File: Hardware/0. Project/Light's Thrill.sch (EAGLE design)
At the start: 41 parts, among them CN1 Micro-USB, CN2 2.1MMJACKTHM, CN3 2x3, Q1 SI2302DS, Q2 SI2302DS, Q3 SI2302DS, U1 TSOP1838, U2 ATMEGA32U4, U3 LM1117-5.0, Y1 16 MHz

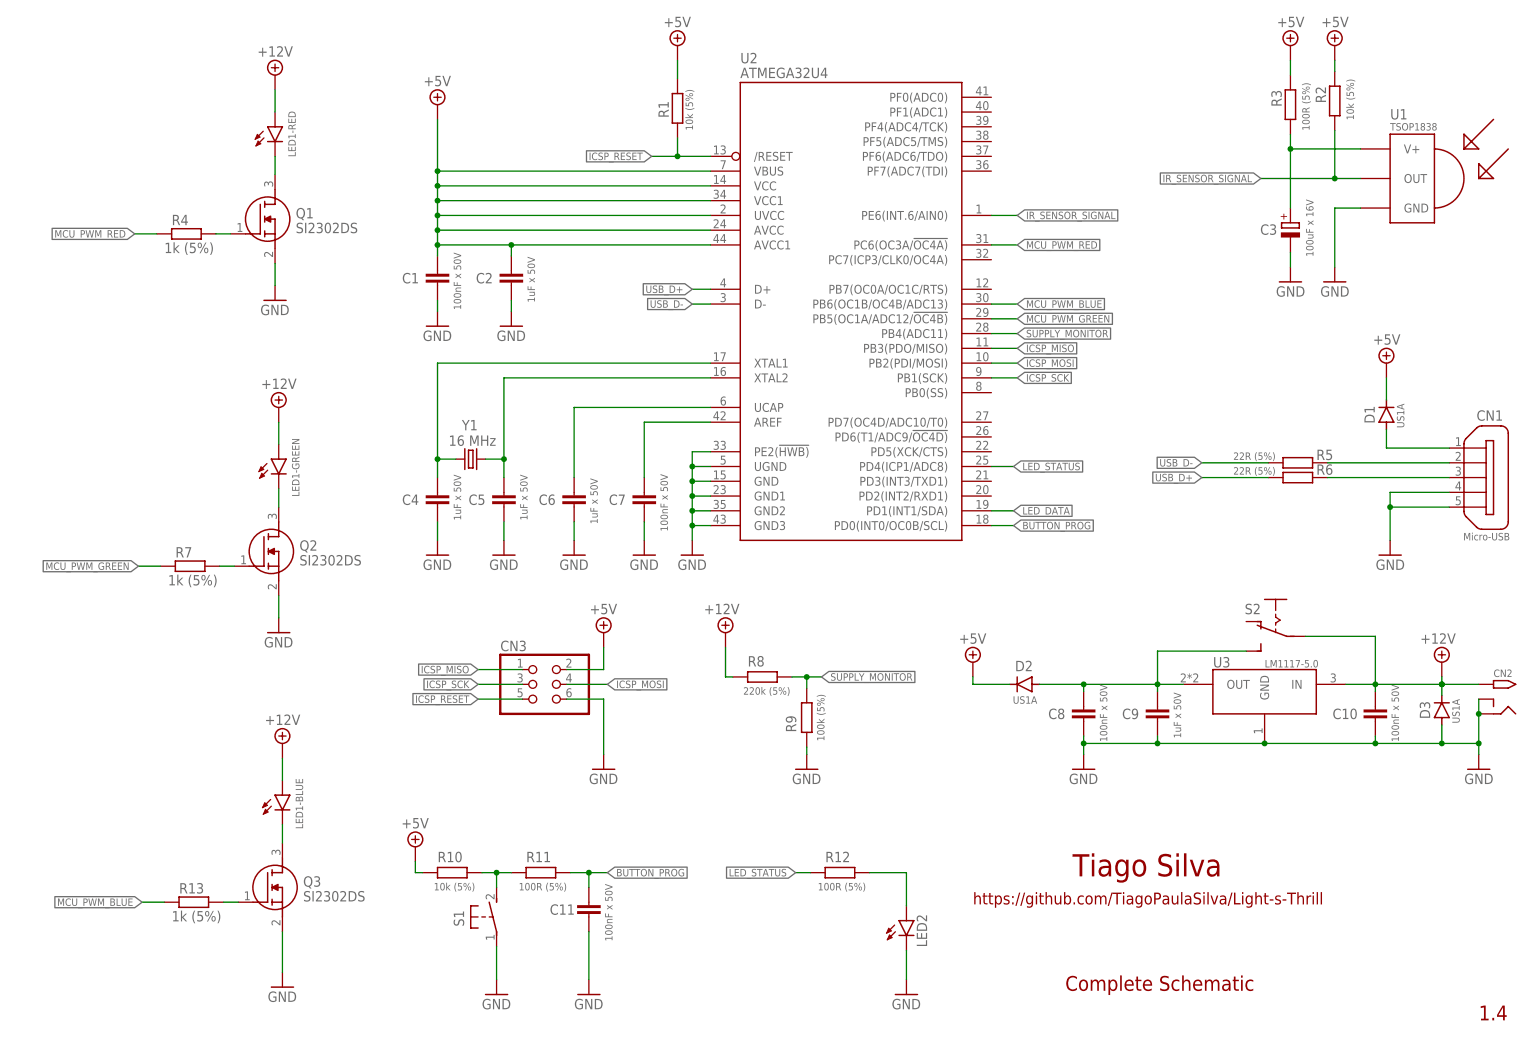
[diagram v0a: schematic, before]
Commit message: New images and directory structure
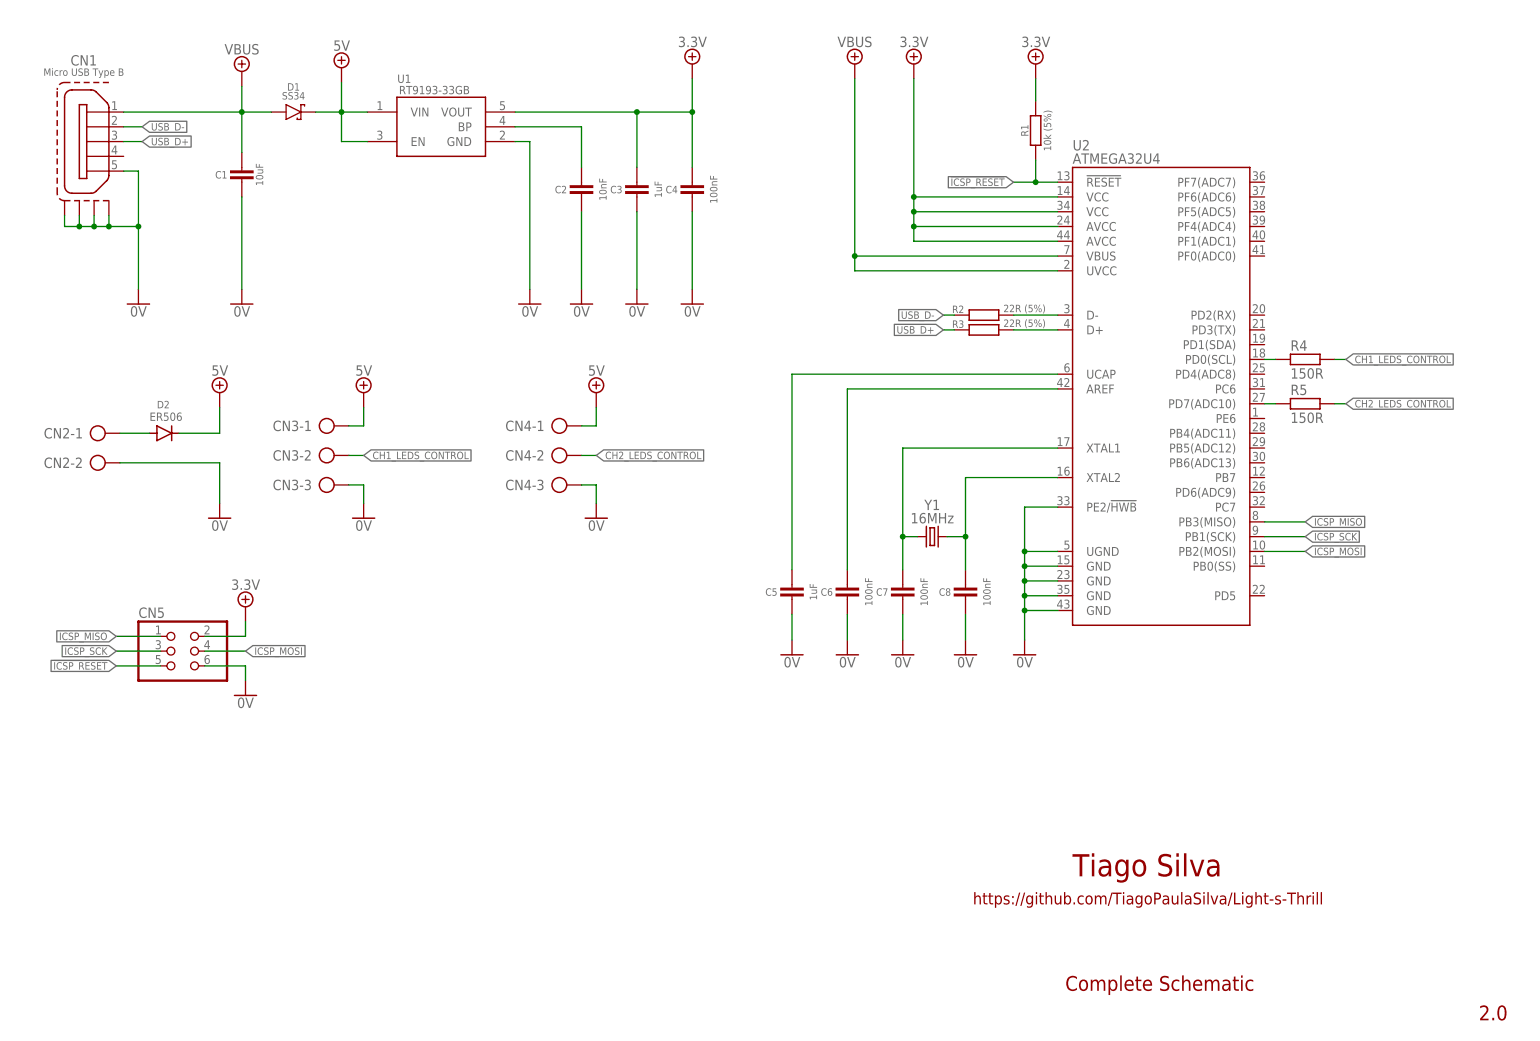
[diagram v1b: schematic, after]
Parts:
- removed C10, C11: 100nF x 50V, rcl:C-EUC0805
- removed C9: 1uF x 50V, rcl:C-EUC0805
- removed D3: US1A, diode:CGRM4007-G
- removed LED1: RGB_LED_STRIP, led:RGB_LED_STRIP
- removed LED2: Red, led:LEDCHIPLED_0805
- removed Q1, Q2, Q3: SI2302DS, SI2302DS:SI2302DS
- removed R10: 10k (5%), rcl:R-EU_R0805
- removed R11, R12: 100R (5%), rcl:R-EU_R0805
- removed R13, R7: 1k (5%), rcl:R-EU_R0805
- removed R6: 22R (5%), rcl:R-EU_R0805
- removed R8: 220k (5%), rcl:R-EU_R0805
- removed R9: 100k (5%), rcl:R-EU_R0805
- removed S1: DTSM-3, switch-tact2:DTSM-3
- removed S2: (no value), switch-HH-NO-MODEL:255SB
- removed U3: LM1117-5.0, LM1117IMP-5.0-NOPB:LM1117IMP-5.0-NOPB
- added CN4: (no value), con-ptr500:AK500/3-H
- added CN5: (no value), pinhead:PINHD-2X3
- C1: value 100nF x 50V -> 10uF; device rcl:C-EUC0805 -> My-RLC:C_0805
- C2: value 1uF x 50V -> 10nF; device rcl:C-EUC0805 -> My-RLC:C_0603
- C3: value 100uF x 16V -> 1uF; device rcl:CPOL-EUE2-5 -> My-RLC:C_0603
- C4, C6: value 1uF x 50V -> 100nF; device rcl:C-EUC0805 -> My-RLC:C_0603
- C5: value 1uF x 50V -> 1uF; device rcl:C-EUC0805 -> My-RLC:C_0603
- C7, C8: value 100nF x 50V -> 100nF; device rcl:C-EUC0805 -> My-RLC:C_0603
- CN1: value Micro-USB -> Micro USB Type B; device Micro USB Connector:ZX62D-B-5PA8 -> My-Connectors:MICRO-USB
- CN2: value 2.1MMJACKTHM -> (none); device adafruit:2.1MMJACKTHM -> con-ptr500:AK500/2-H
- CN3: value 2x3 -> (none); device pinhead:PINHD-2X3 -> con-ptr500:AK500/3-H
- D1: value US1A -> SS34; device diode:CGRM4007-G -> My-Diodes:SS34
- D2: value US1A -> ER506; device diode:CGRM4007-G -> diode:BY550
- R1: device rcl:R-EU_R0805 -> My-RLC:R_0603
- R2: value 10k (5%) -> 22R (5%); device rcl:R-EU_R0805 -> My-RLC:R_0603
- R3: value 100R (5%) -> 22R (5%); device rcl:R-EU_R0805 -> My-RLC:R_0603
- R4: value 1k (5%) -> 150R; device rcl:R-EU_R0805 -> My-RLC:R_0603
- R5: value 22R (5%) -> 150R; device rcl:R-EU_R0805 -> My-RLC:R_0603
- U1: value TSOP1838 -> RT9193-33GB; device TSOP1838:TSOP1838 -> RT9193-33GB:RT9193-33GB
- U2: device adafruit:ATMEGA32U4-AU -> SparkFun_Pro_Micro_v13a:TESTING_ATMEGA32U4QFN
- Y1: value 16 MHz -> 16MHz
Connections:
- removed net +12V: C10.1, CN2.TIP, D3.C, LED1G$4.ANODE, R8.2, S2.P, U3.IN
- removed net +5V: C1.1, C2.1, CN3.2, D1.C, D2.C, R1.2, R10.1, R2.1, R3.1, U2.AVCC, U2.AVCC1, U2.UVCC, U2.VBUS, U2.VCC, U2.VCC1
- removed net BUTTON_PROG: C11.1, R11.1, U2.PD0(INT0/OC0B/SCL)
- removed net GND: C1.2, C10.2, C11.2, C2.2, C3.-, C4.2, C5.2, C6.2, C7.2, C8.2, C9.2, CN1G$1.4, CN1G$1.5, CN2.RING, CN2.RING_SW, CN3.6, D3.A, LED2.C, Q1.S, Q2.S, Q3.S, R9.1, S1.1, U1.GND, U2.GND, U2.GND1, U2.GND2, U2.GND3, U2.PE2(!HWB), U2.UGND, U3.GND
- removed net ICSP_RESET: CN3.5, R1.1, U2./RESET
- removed net IR_SENSOR_SIGNAL: R2.2, U1.OUT, U2.PE6(INT.6/AIN0)
- removed net LED_DATA: U2.PD1(INT1/SDA)
- removed net LED_STATUS: R12.1, U2.PD4(ICP1/ADC8)
- removed net MCU_PWM_BLUE: R13.1, U2.PB6(OC1B/OC4B/ADC13)
- removed net MCU_PWM_GREEN: R7.1, U2.PB5(OC1A/ADC12/!OC4B)
- removed net MCU_PWM_RED: R4.1, U2.PC6(OC3A/!OC4A)
- removed net N$1: Q1.G, R4.2
- removed net N$11: C6.1, U2.UCAP
- removed net N$13: C4.1, U2.XTAL1, Y1.1
- removed net N$14: C5.1, U2.XTAL2, Y1.2
- removed net N$2: LED1-RED.C, Q1.D
- removed net N$4: Q3.G, R13.2
- removed net N$5: LED1-GREEN.C, Q2.D
- removed net N$8: CN1G$1.2, R5.2
- removed net N$9: CN1G$1.3, R6.2
- removed net SUPPLY_MONITOR: R8.1, R9.2, U2.PB4(ADC11)
- new net !ICSP_RESET: CN5.5, R1.1, U2.!RESET
- new net 0V: C1.2, C2.2, C3.2, C4.2, C5.2, C6.2, C7.2, C8.2, CN1G$1.5, CN1G$2.S1, CN1G$2.S2, CN1G$2.S3, CN1G$2.S4, CN2-2.KL, CN3-3.KL, CN4-3.KL, CN5.6, U1.GND, U2.GND@15, U2.GND@23, U2.GND@35, U2.GND@43, U2.PE2/!HWB, U2.UGND
- new net 3.3V: C3.1, C4.1, CN5.2, R1.2, U1.VOUT, U2.AVCC@24, U2.AVCC@44, U2.VCC@14, U2.VCC@34
- new net 5V: CN3-1.KL, CN4-1.KL, D1.K, D2.C, U1.EN, U1.VIN
- new net CH1_LEDS_CONTROL: CN3-2.KL, R4.2
- new net CH2_LEDS_CONTROL: CN4-2.KL, R5.2
- new net N$20: R2.2, U2.D-
- new net N$21: C2.1, U1.BP
- new net VBUS: C1.1, CN1G$1.1, D1.A, U2.UVCC, U2.VBUS
- net ICSP_MISO: now also CN5.1, U2.PB3(MISO); no longer CN3.1, U2.PB3(PDO/MISO)
- net ICSP_MOSI: now also CN5.4, U2.PB2(MOSI); no longer CN3.4, U2.PB2(PDI/MOSI)
- net ICSP_SCK: now also CN5.3; no longer CN3.3
- net N$12: now also R3.2, U2.D+; no longer C7.1, U2.AREF
- net N$15: now also C7.1, U2.XTAL1, Y1.1; no longer CN1G$1.1, D1.A
- net N$16: now also U2.XTAL2, Y1.2; no longer C9.1, D2.A, S2.S, U3.OUT
- net N$17: now also C5.1, U2.UCAP; no longer R10.2, R11.2, S1.2
- net N$18: now also C6.1, U2.AREF; no longer LED2.A, R12.2
- net N$3: now also R4.1, U2.PD0(SCL); no longer Q2.G, R7.2
- net N$6: now also CN2-1.KL, D2.A; no longer LED1-BLUE.C, Q3.D
- net N$7: now also R5.1, U2.PD7(ADC10); no longer C3.+, R3.2, U1.V+
- net USB_D+: now also CN1G$1.3, R3.1; no longer R6.1, U2.D+
- net USB_D-: now also CN1G$1.2, R2.1; no longer R5.1, U2.D-
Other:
- note added: "2.0"
- note removed: "1.4"
- note removed: "BLUE"
- note removed: "D10"
- note removed: "D2"
- note removed: "D3"
- note removed: "D4"
- note removed: "D5"
- note removed: "D7"
- note removed: "D8"
- note removed: "D9"
- note removed: "GREEN"
- note removed: "RED"
- moved on the sheet: C1, C2, C4, C5, C6, C7, C8, CN1, D2, R1, R2, R3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
